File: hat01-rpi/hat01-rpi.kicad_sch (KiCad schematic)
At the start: 58 parts, among them J1 Network Connector, J2 RPi_4B_GPIO_Header, J3 USB_A, J4 Conn_01x03, SW1 SW_Push, U1 MCP2515-xSO, U2 TPS5430DDA, U3 SN65HVD230, Y1 8MHz

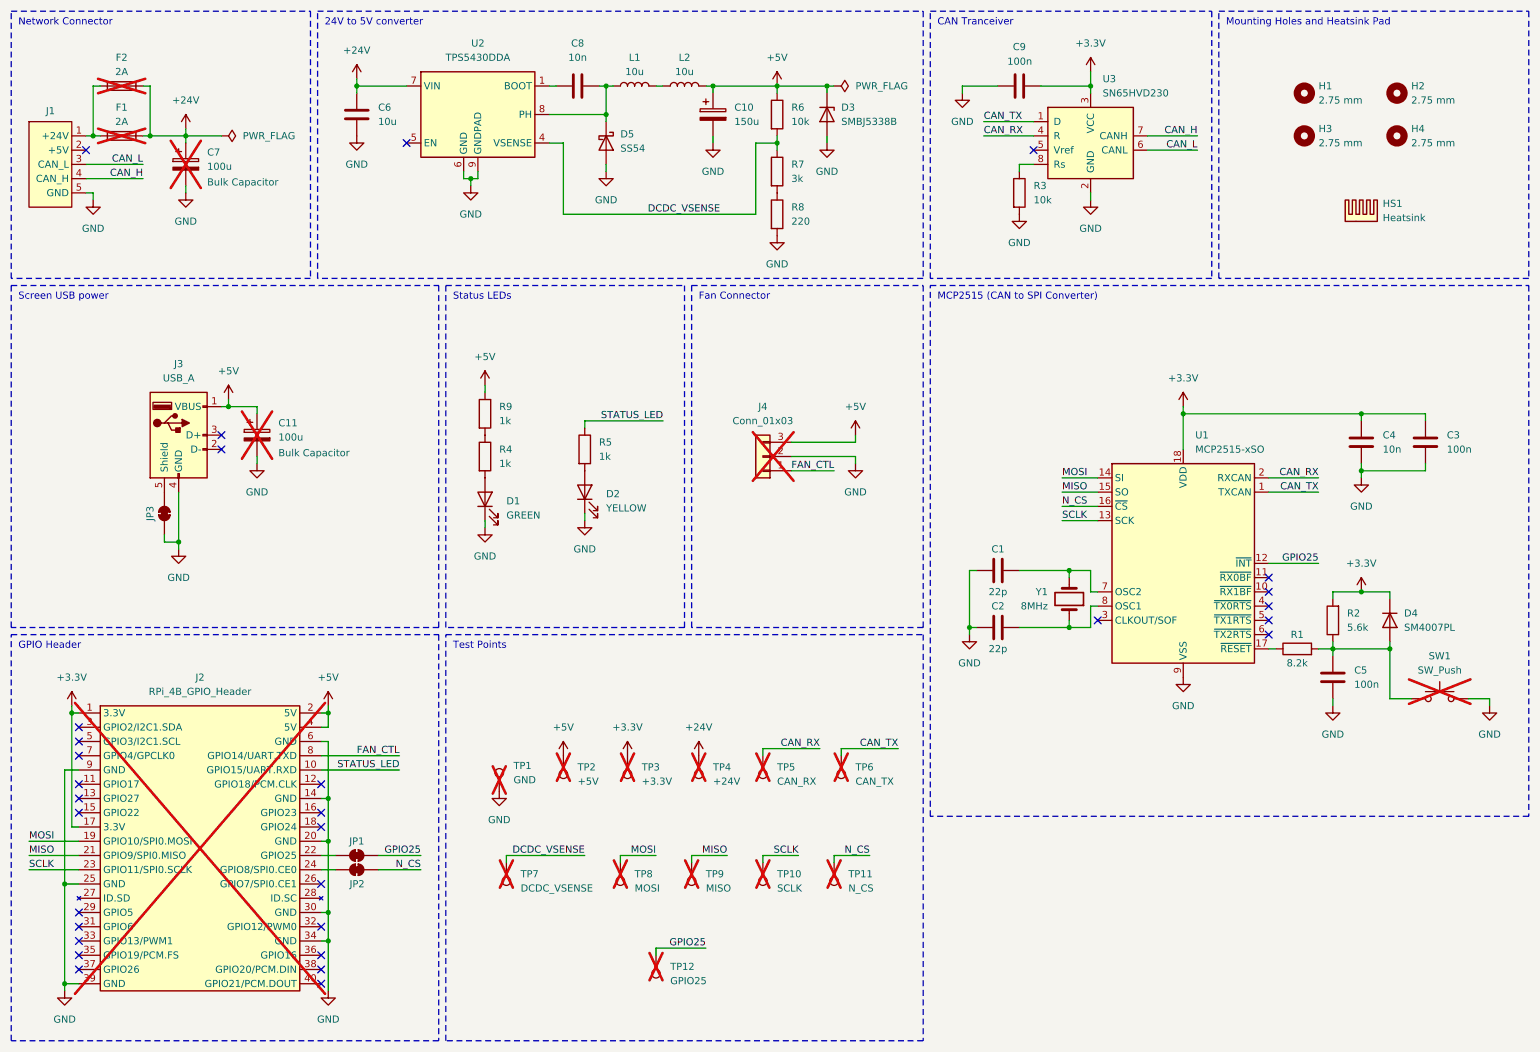
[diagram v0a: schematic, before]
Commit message: hat01-rpi: finish board layout
All components placed and routed.

Could improve:
- Some traces could be rouned around edges
- Some traces should be more parallel (and same length)
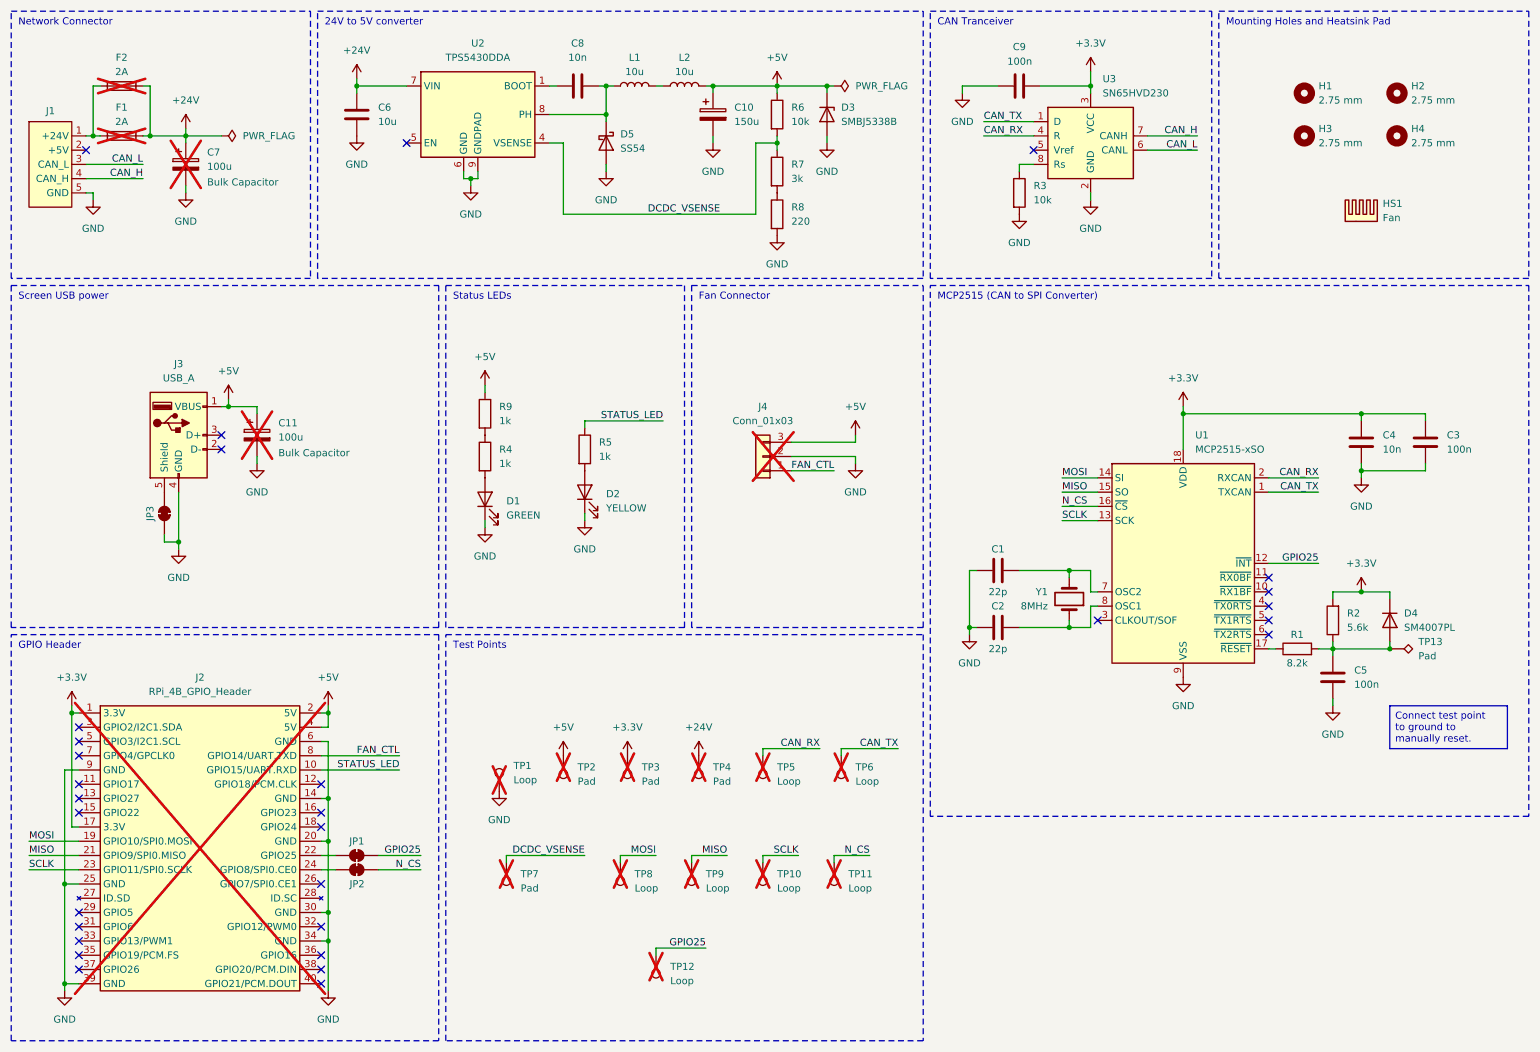
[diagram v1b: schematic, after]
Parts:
- removed SW1: SW_Push, Button_Switch_THT:SW_PUSH_6mm, symbol Switch:SW_Push
- added TP13: Pad, TestPoint:TestPoint_Pad_D1.5mm, symbol Connector:TestPoint_Alt
- C1, C2: footprint Capacitor_SMD:C_0603_1608Metric_Pad1.08x0.95mm_HandSolder -> Capacitor_SMD:C_0402_1005Metric; JLCPCB C1653 -> C1555
- HS1: value Heatsink -> Fan; footprint (none) -> Exocet:RPi_Fan_Mount
- R8: footprint Resistor_SMD:R_0603_1608Metric_Pad0.98x0.95mm_HandSolder -> Resistor_SMD:R_0402_1005Metric; JLCPCB C22962 -> C25091
- TP1: value GND -> Loop
- TP10: value SCLK -> Loop
- TP11: value N_CS -> Loop
- TP12: value GPIO25 -> Loop
- TP2: value +5V -> Pad; footprint TestPoint:TestPoint_Keystone_5005-5009_Compact -> TestPoint:TestPoint_Pad_D1.5mm
- TP3: value +3.3V -> Pad; footprint TestPoint:TestPoint_Keystone_5005-5009_Compact -> TestPoint:TestPoint_Pad_D1.5mm
- TP4: value +24V -> Pad; footprint TestPoint:TestPoint_Keystone_5005-5009_Compact -> TestPoint:TestPoint_Pad_D1.5mm
- TP5: value CAN_RX -> Loop
- TP6: value CAN_TX -> Loop
- TP7: value DCDC_VSENSE -> Pad; footprint TestPoint:TestPoint_Keystone_5005-5009_Compact -> TestPoint:TestPoint_Pad_D1.5mm
- TP8: value MOSI -> Loop
- TP9: value MISO -> Loop
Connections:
- net at C5.1, D4.2 (A), R1.2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: now also TP13.1

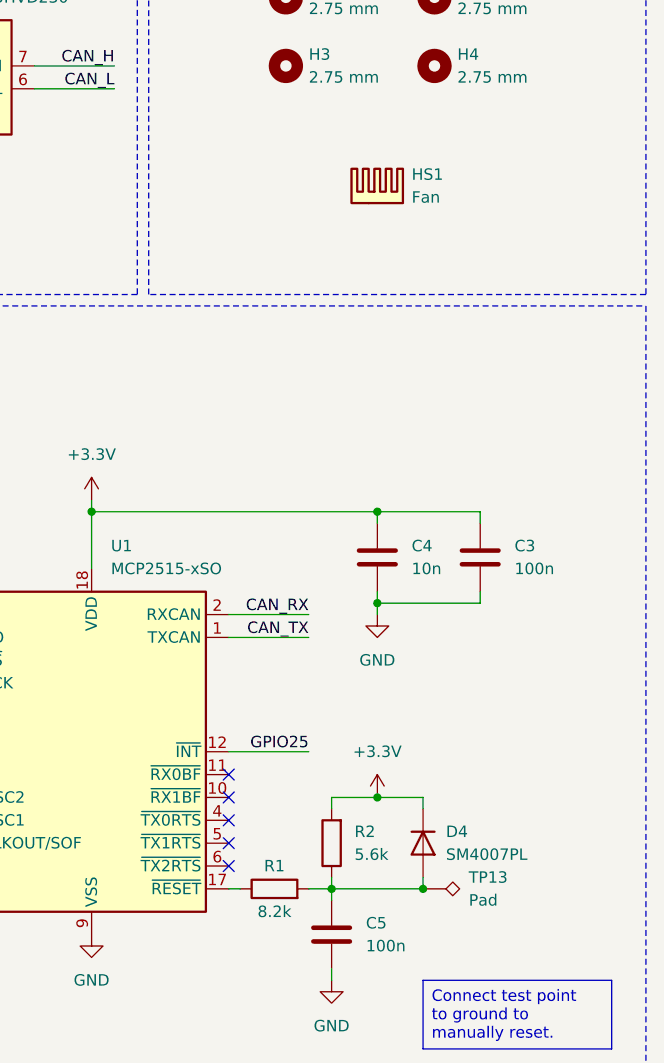
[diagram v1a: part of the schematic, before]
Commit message: hat01-rpi: minors improvements to board part data
Some components needed to be marked as DNP/exclude from BOM. Finished
rounding some traces around corners. Added some information on the
Silkscreen. This commit was not directly used for the order (this is
v1.1.1, not v1.1.0), but some modifications were added to the previous
version before the order.
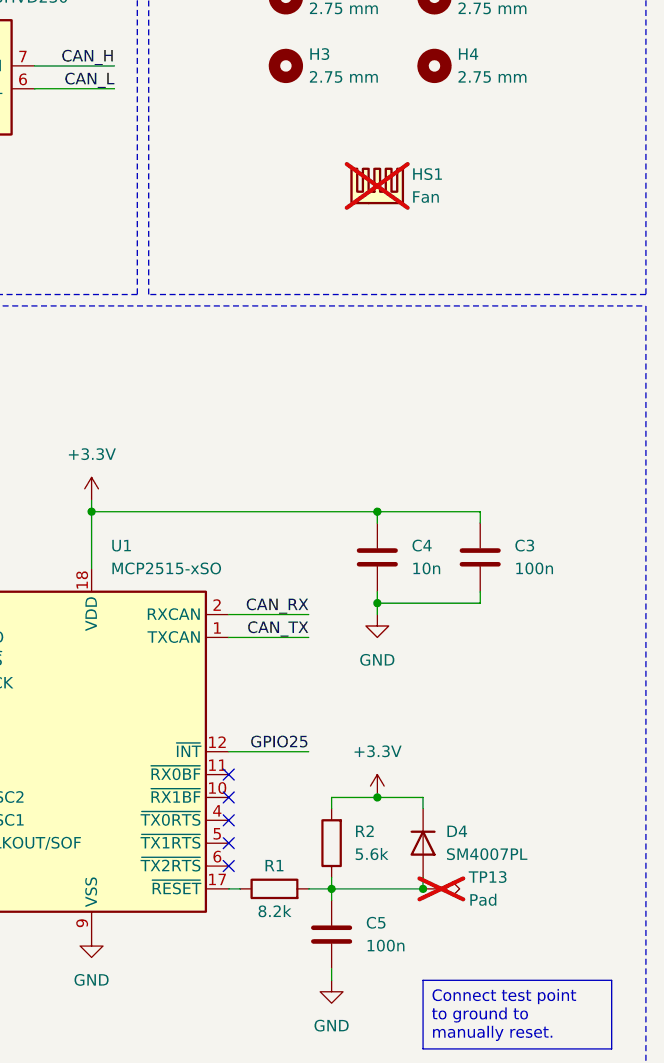
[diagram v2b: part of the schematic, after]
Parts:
- HS1, TP13: now not fitted
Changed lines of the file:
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@@
 		(title "Main page")
 		(date "2026-04-04")
-		(rev "v1.1.0")
+		(rev "v1.1.1")
 	)
 	(rectangle
@@
 		(in_bom yes)
 		(on_board yes)
-		(dnp no)
+		(dnp yes)
 		(fields_autoplaced yes)
 		(property "Reference" "TP13"
@@
 		(in_bom no)
 		(on_board yes)
-		(dnp no)
+		(dnp yes)
 		(fields_autoplaced yes)
 		(property "Reference" "HS1"

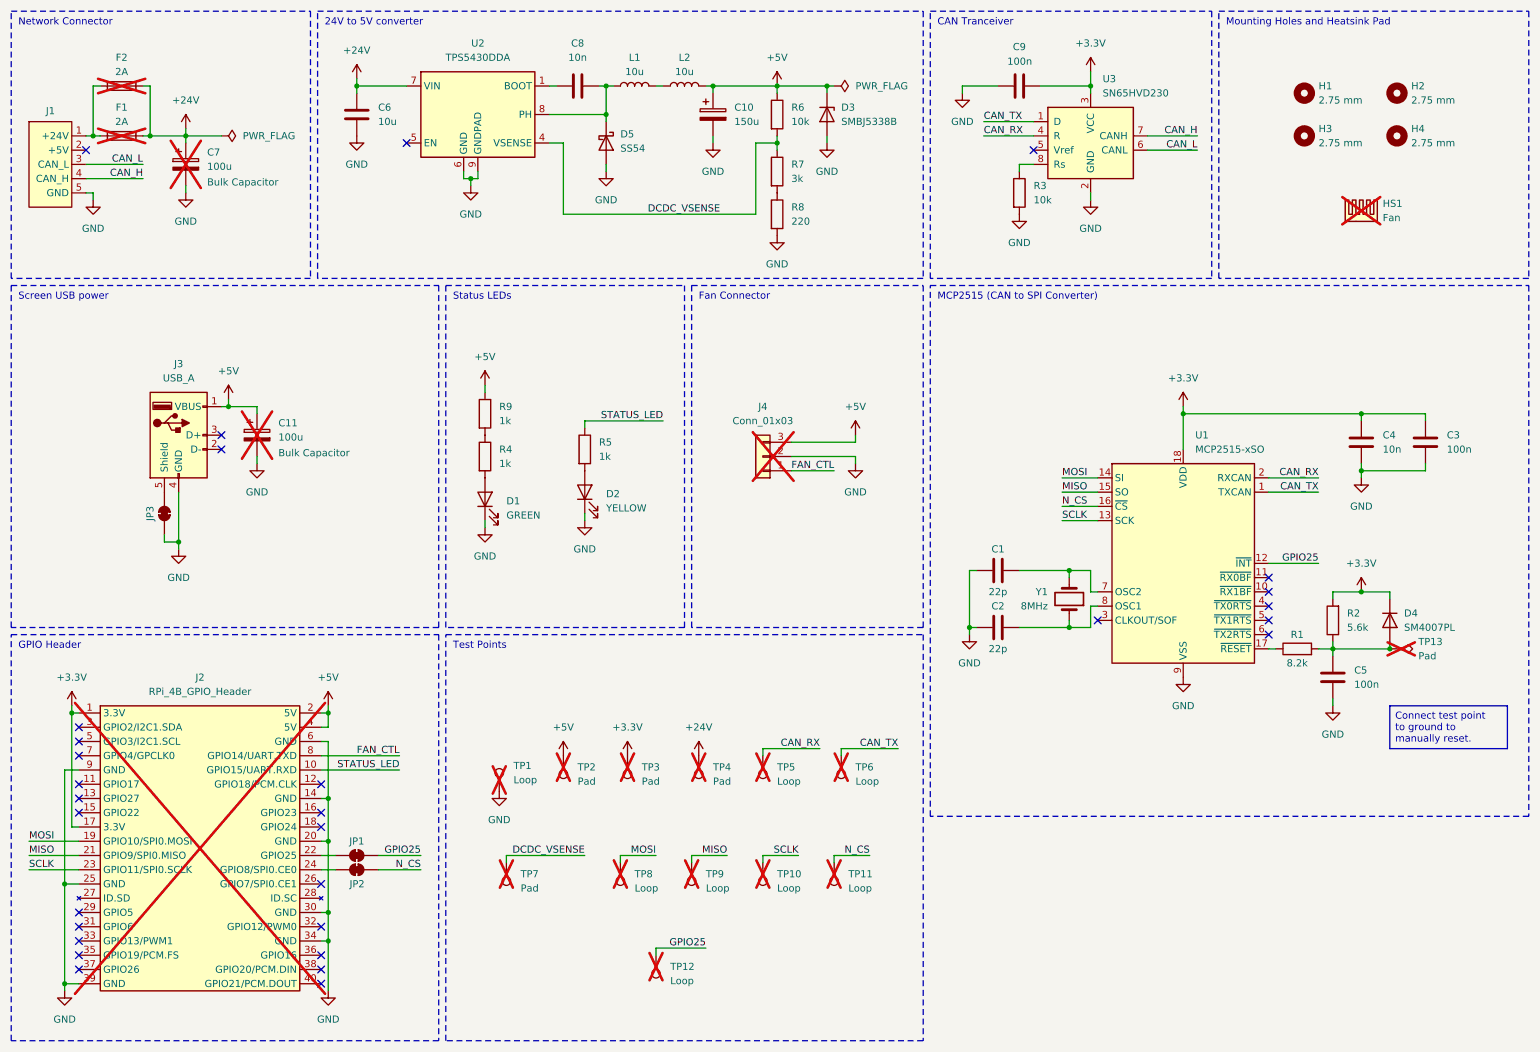
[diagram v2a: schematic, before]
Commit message: hat01-rpi: Mark D3 and DNP
This diode's zener voltage was too low and would conduct in normal
operation. It was removed since it would heat up and is not particularly
useful.
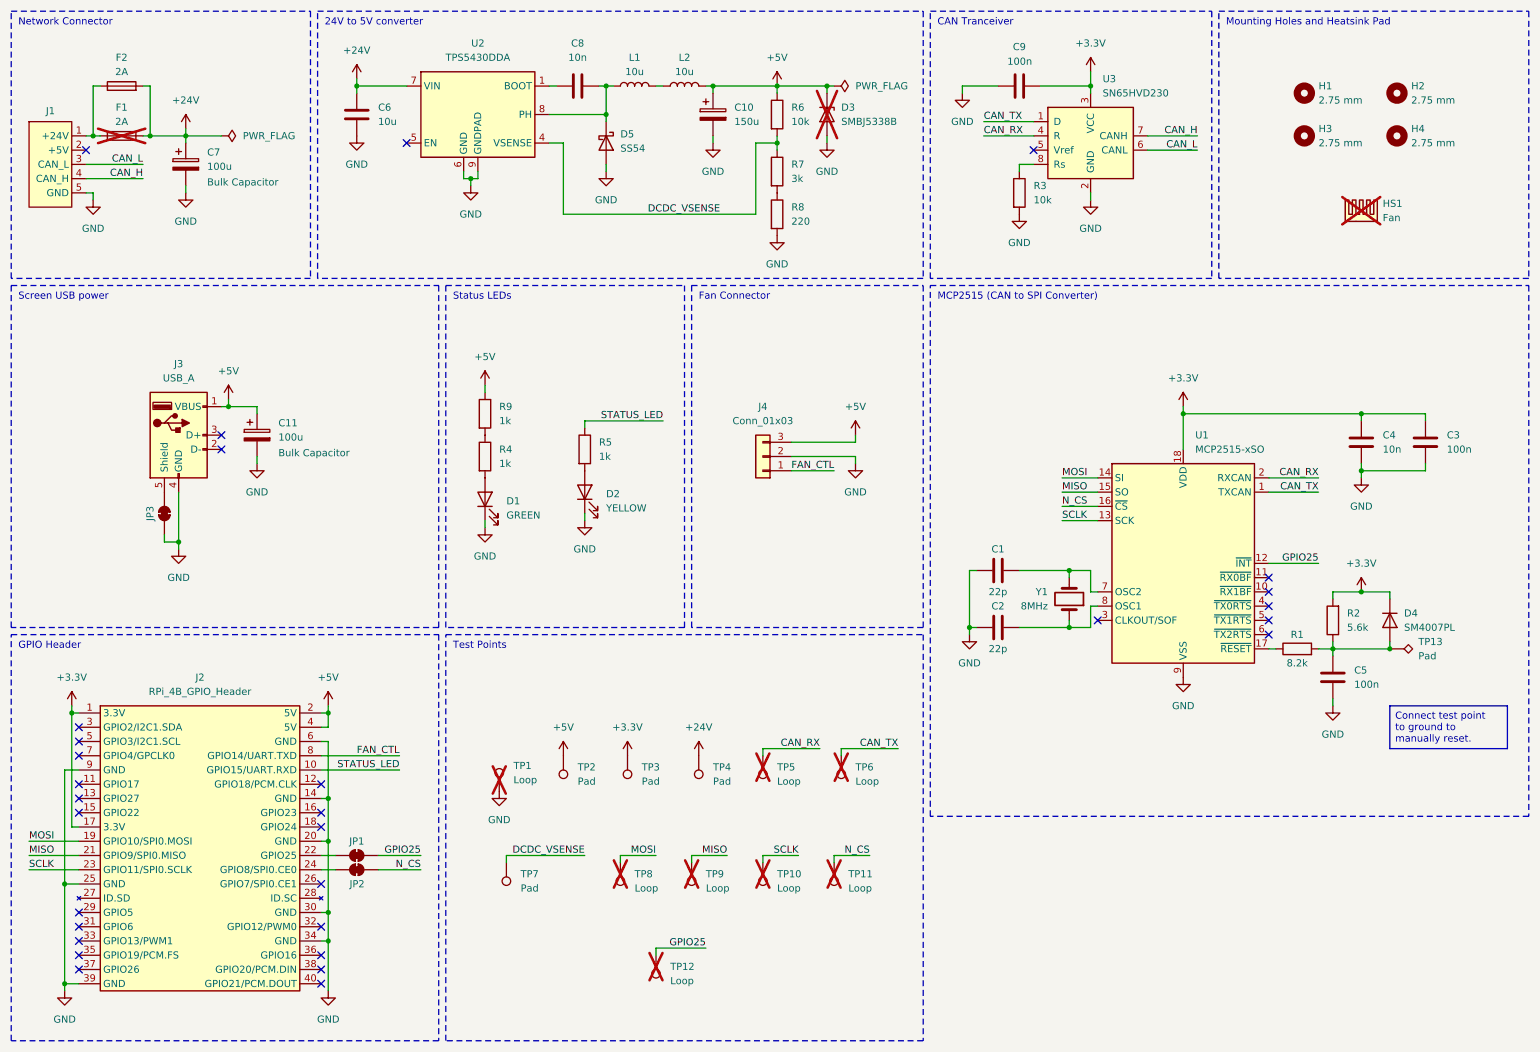
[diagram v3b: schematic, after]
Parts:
- C11, C7, F2, J2, J4, TP13, TP2, TP3, TP4, TP7: now fitted
- D3: now not fitted
